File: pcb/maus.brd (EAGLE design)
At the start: 100 x 101 mm, 79 parts, among them IC1 AP1509-50SG-13, J1 SS-52300-001, Q2 BSS123, Q3 BSS123, Q4 BSS123, Q6 PMN30XPEA, Q7 PMN30XPEA, U2 CH340C, U4 LP3965EMP-3.3, U6 LM358DR, U69 ESP32-S2-WROOM

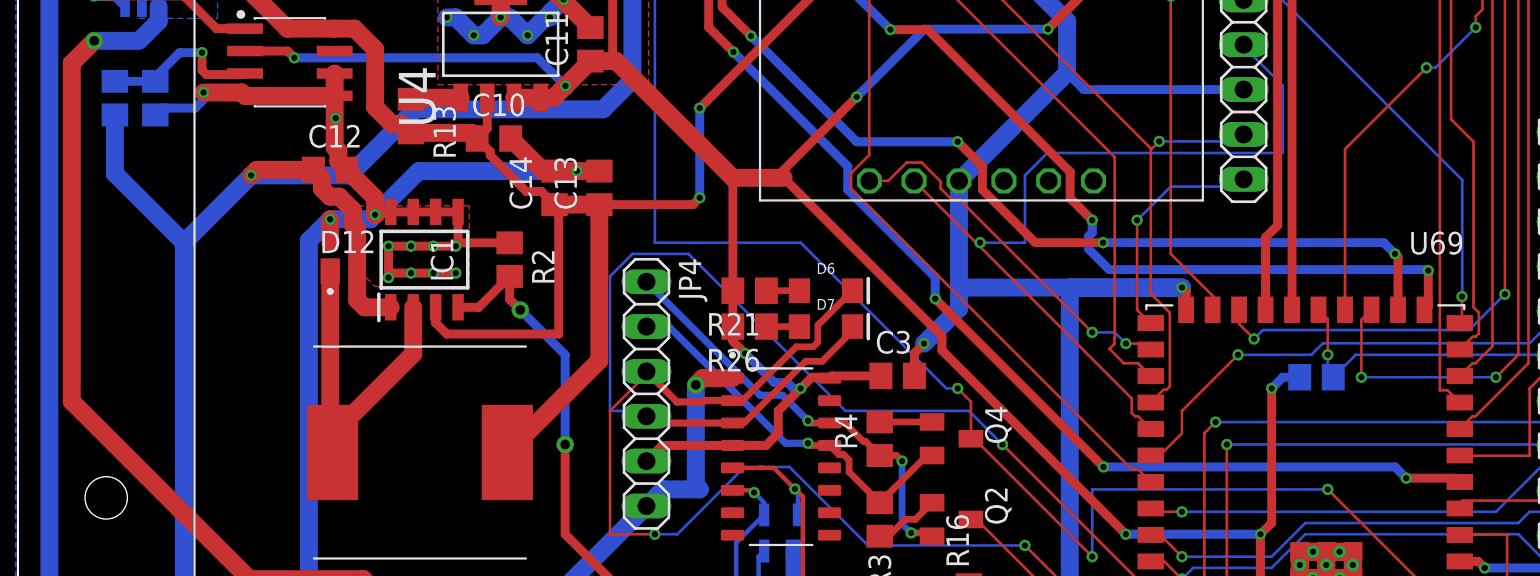
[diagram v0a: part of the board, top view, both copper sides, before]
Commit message: removed wire stubs
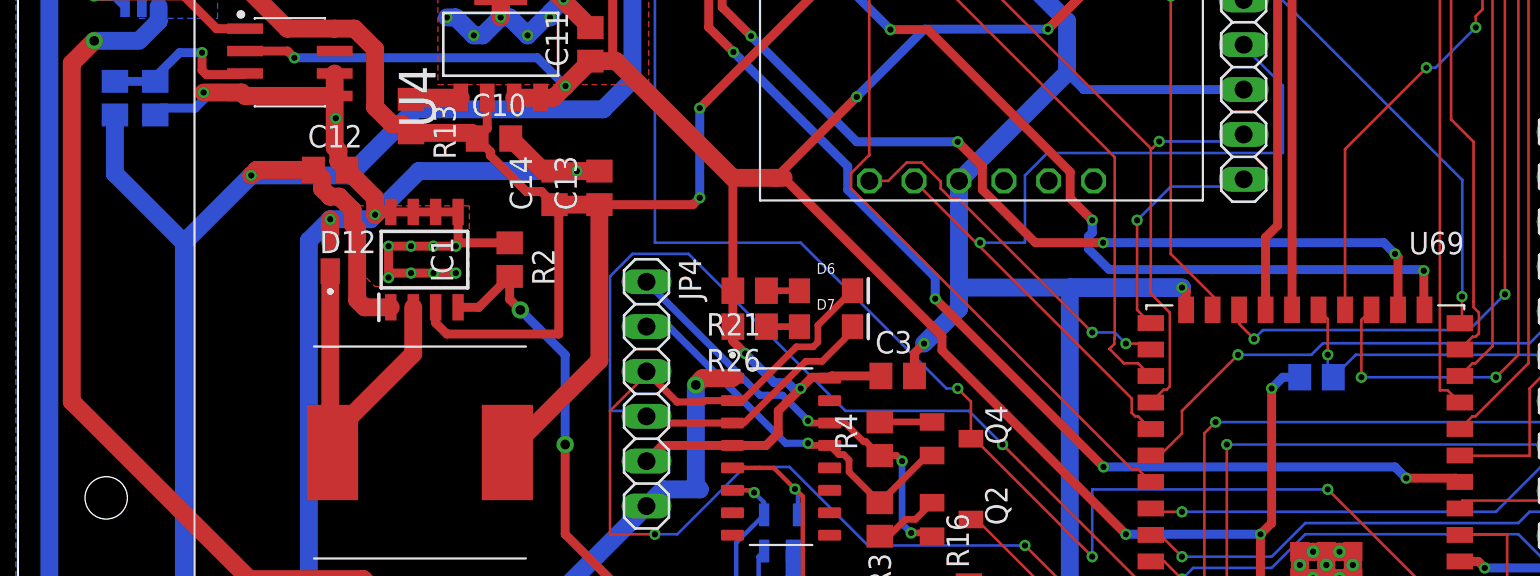
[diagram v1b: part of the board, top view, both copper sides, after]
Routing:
- net ESP32_M2_CH_B: track 51.4 -> 50.7 mm
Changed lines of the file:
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@@
 <wire x1="76.835" y1="45.01204375" x2="76.618" y2="44.79504375" width="0.508" layer="16"/>
 <wire x1="76.618" y1="44.10495625" x2="77.79695625" y2="42.926" width="0.508" layer="16"/>
-<wire x1="95.885" y1="42.8423" x2="95.8648" y2="42.8625" width="0.508" layer="16"/>
-<via x="95.8648" y="42.8625" extent="1-16" drill="0.35"/>
-<wire x1="95.8648" y1="42.8625" x2="95.8648" y2="40.8648" width="0.508" layer="1"/>
-<wire x1="95.8648" y1="40.8648" x2="95.65" y2="40.65" width="0.508" layer="1"/>
-<wire x1="77.79695625" y1="42.926" x2="95.8013" y2="42.926" width="0.508" layer="16"/>
-<wire x1="95.8013" y1="42.926" x2="95.8648" y2="42.8625" width="0.508" layer="16"/>
+<via x="95.6108" y="42.8625" extent="1-16" drill="0.35"/>
+<wire x1="95.65" y1="40.65" x2="95.6108" y2="40.6892" width="0.508" layer="1"/>
+<wire x1="95.6108" y1="42.8625" x2="95.6108" y2="40.6892" width="0.508" layer="1"/>
+<wire x1="77.79695625" y1="42.926" x2="95.5473" y2="42.926" width="0.508" layer="16"/>
+<wire x1="95.5473" y1="42.926" x2="95.6108" y2="42.8625" width="0.508" layer="16"/>
 </signal>
 <signal name="ESP32_M1_2">
@@
 <wire x1="45.085" y1="86.995" x2="71.755" y2="86.995" width="0.15" layer="1"/>
 <wire x1="45.085" y1="86.995" x2="44.85" y2="87.49" width="0.15" layer="1"/>
-<wire x1="85.15" y1="40.2012375" x2="85.15" y2="40.65" width="0.1524" layer="1"/>
 <via x="78.74" y="81.915" extent="1-16" drill="0.35"/>
 <wire x1="85.15" y1="40.65" x2="85.15" y2="39.85" width="0.1524" layer="1"/>
@@
 <wire x1="98.552" y1="57.277" x2="98.552" y2="56.642" width="0.15" layer="1"/>
 <wire x1="95.885" y1="84.455" x2="98.679" y2="84.455" width="0.15" layer="16"/>
-<wire x1="91.44" y1="41.275" x2="91.15" y2="40.65" width="0.15" layer="1"/>
 <wire x1="95.885" y1="84.455" x2="95.5" y2="84.76" width="0.15" layer="16"/>
 <via x="98.679" y="84.455" extent="1-16" drill="0.35"/>
@@
 <contactref element="U2" pad="5"/>
 <wire x1="56.464" y1="31.697" x2="58" y2="31.697" width="0.254" layer="1" grouprefs="USB"/>
-<wire x1="58" y1="31.697" x2="58.198" y2="31.697" width="0.254" layer="1" grouprefs="USB"/>
 <wire x1="60.444" y1="30.086" x2="60.444" y2="22.934" width="0.254" layer="1" grouprefs="USB"/>
 <wire x1="58" y1="31.697" x2="58.803" y2="31.697" width="0.254" layer="1"/>
@@
 <wire x1="29.75" y1="74.93" x2="29.75" y2="68.58" width="0.508" layer="1" grouprefs="MOTOR_LINKS"/>
 <wire x1="87.17" y1="69.19" x2="87.17" y2="75.78" width="0.508" layer="1"/>
-<wire x1="21.494" y1="51.684" x2="21.59" y2="51.588" width="1.016" layer="16"/>
 <wire x1="25.276" y1="19.378" x2="25.4" y2="19.502" width="1.016" layer="16"/>
 <via x="29.21" y="48.26" extent="1-16" drill="0.35"/>

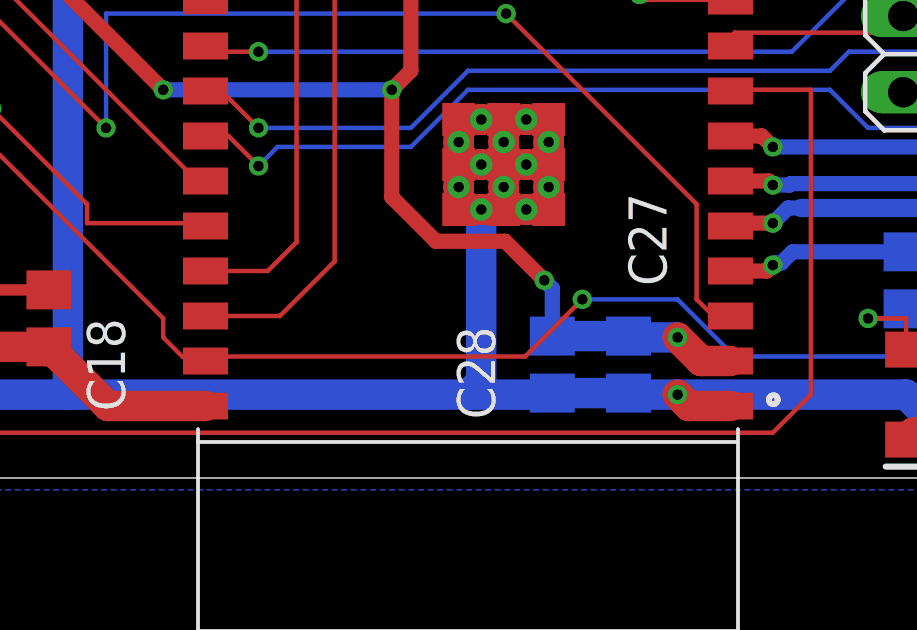
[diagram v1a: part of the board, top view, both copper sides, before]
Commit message: via am C27
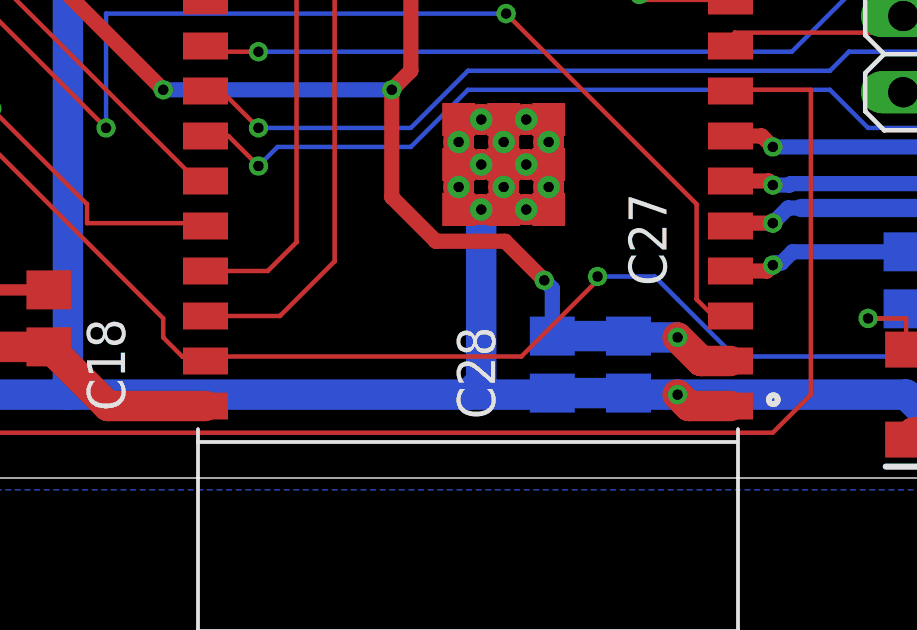
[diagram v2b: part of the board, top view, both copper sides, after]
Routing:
- net ESP32_EN: track 217.9 -> 219.0 mm

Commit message: meeting mit alex
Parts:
- moved YRMOM 14.6 mm to (42.4, 77.0), flipped to the bottom, turned to 90 degrees
- moved D8 13.3 mm to (42.4, 69.2), flipped to the bottom, turned to 90 degrees
- moved SV2 13.2 mm to (42.1, 73.0), turned to 180 degrees
- moved D11 12.3 mm to (47.1, 77.0), flipped to the bottom, turned to 90 degrees
- moved D10 10.8 mm to (47.2, 69.2), flipped to the bottom, turned to 90 degrees
- moved C9 1.92 mm to (55.4, 72.3), flipped to the bottom
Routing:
- net +3V3: track 268.2 -> 227.0 mm
- net M1_M+: track 57.2 -> 20.9 mm, vias 3 -> 0
- net VBAT: track 229.5 -> 195.5 mm, vias 7 -> 8
- net M1_M-: track 54.3 -> 21.0 mm, vias 2 -> 0
- net ESP32_M1_CH_A: track 115.4 -> 88.2 mm
- net GND: track 849.6 -> 826.5 mm, vias 34 -> 32
- net ESP32_M1_CH_B: track 75.8 -> 54.8 mm

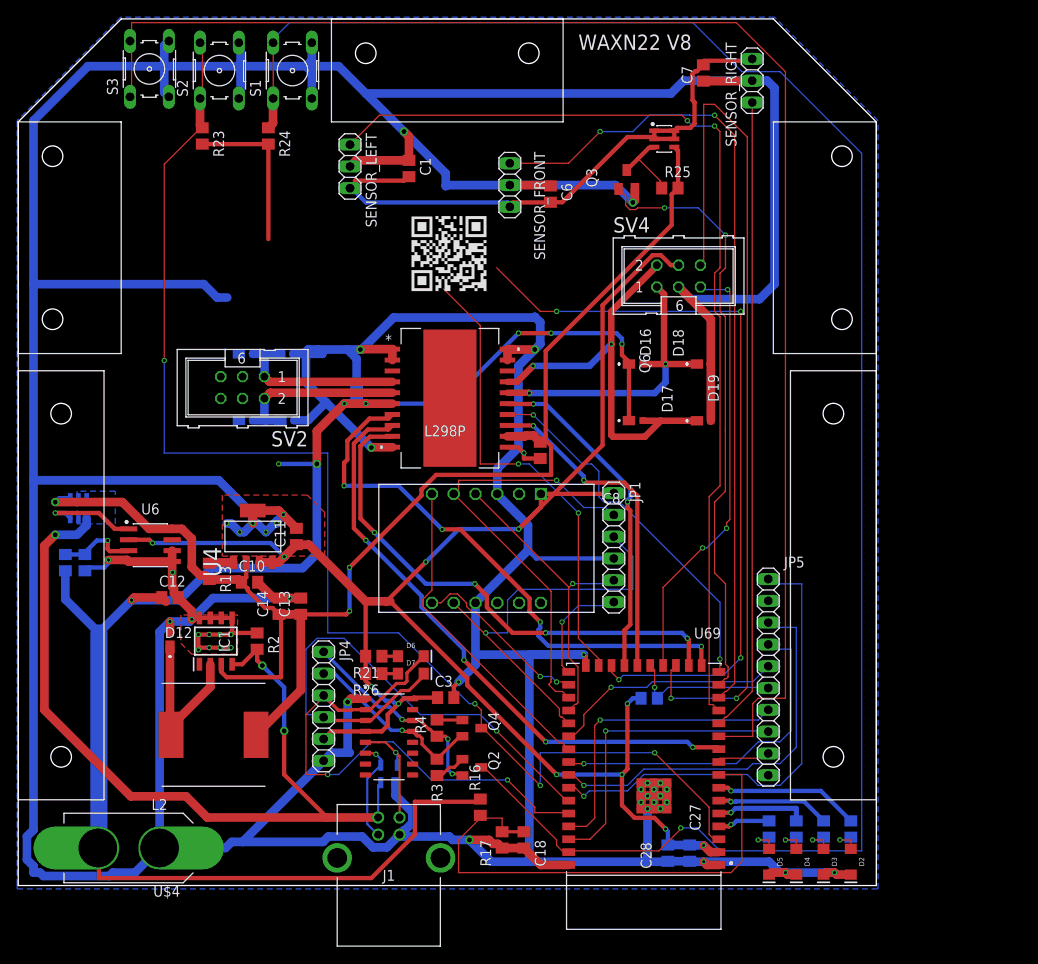
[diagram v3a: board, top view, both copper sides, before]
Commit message: feat: update hbridge, connectors and add motor overlap
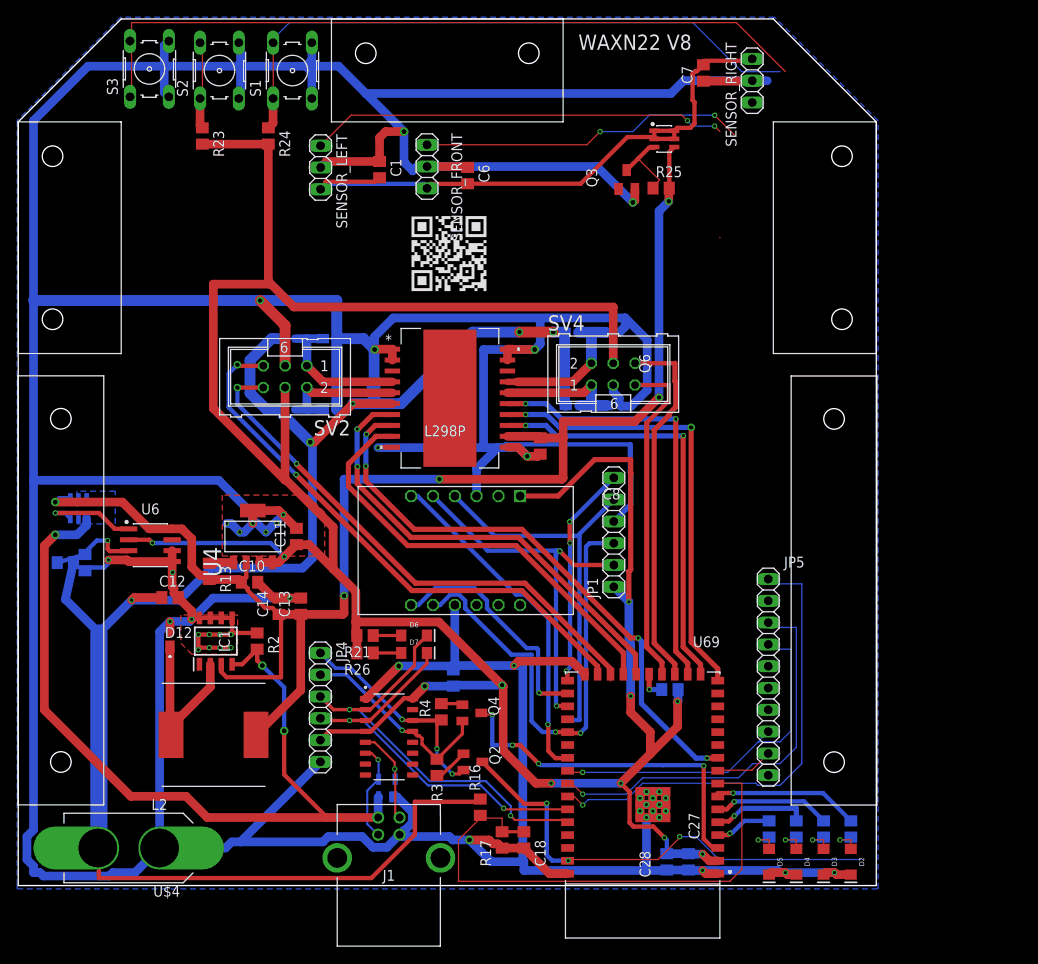
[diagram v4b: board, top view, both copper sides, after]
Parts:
- removed U$5: (no value), shared:MOTOR_HALTERUNG
- added U$3: (no value), maus:MOTOR_HALTERUNG
- moved U$1 50.4 mm to (16.0, 74.4), turned to 270 degrees
- moved D19 14.8 mm to (85.1, 79.5), flipped to the bottom, turned to 90 degrees
- moved SV4 13.7 mm to (85.3, 74.6)
- moved D17 12.7 mm to (80.3, 79.5), flipped to the bottom, turned to 90 degrees
- moved D18 11.6 mm to (85.2, 71.0), flipped to the bottom, turned to 90 degrees
- moved C6 9.89 mm to (68.4, 97.7)
- moved SENSOR_FRONT 9.89 mm to (63.6, 98.8)
- moved D16 8.81 mm to (80.5, 71.0), flipped to the bottom, turned to 90 degrees
- moved D11 5.38 mm to (52.1, 78.7)
- moved YRMOM 5.26 mm to (47.3, 78.7)
- moved SV2 5.11 mm to (47.1, 74.3)
- moved D10 5.11 mm to (52.1, 70.5)
- moved D8 5.11 mm to (47.3, 70.5)
- moved C1 3.43 mm to (58.1, 98.4)
- moved SENSOR_LEFT 3.43 mm to (51.2, 98.7)
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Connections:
- net ESP32_M1_1: now also U69.22; no longer U69.17
- net ESP32_M1_2: now also U69.23; no longer U69.18
- net ESP32_M2_1: now also U69.17; no longer U69.22
- net ESP32_M2_2: now also U69.18; no longer U69.23
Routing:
- net ESP32_IO0: track 154.1 -> 52.2 mm
- net +3V3: track 227.0 -> 322.2 mm
- net ESP32_EN: track 219.0 -> 128.1 mm, vias 1 -> 3
- net N$1: track 172.2 -> 87.5 mm
- net SENSOR_RIGHT: track 74.1 -> 0.00 mm
- net SENSOR_EN: track 70.1 -> 0.00 mm, vias 2 -> 0
- net SENSOR_LEFT: track 114.6 -> 48.8 mm
- net ESP32_M2_CH_A: track 103.2 -> 43.2 mm, vias 2 -> 0
- net SENSOR_FRONT: track 95.9 -> 38.3 mm
- net IO45: track 35.2 -> 0.77 mm, vias 1 -> 0
- net IO46: track 34.8 -> 1.50 mm, vias 1 -> 0
- net M2_M-: track 48.8 -> 17.5 mm, vias 2 -> 0
- net DRDY_M: track 27.4 -> 0.50 mm, vias 1 -> 0
- net ESP32_M1_CH_A: track 88.2 -> 62.7 mm, vias 4 -> 2
- net M2_M+: track 36.7 -> 15.7 mm, vias 2 -> 0
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
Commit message: Connected GPIO and moved around some cablesÇ
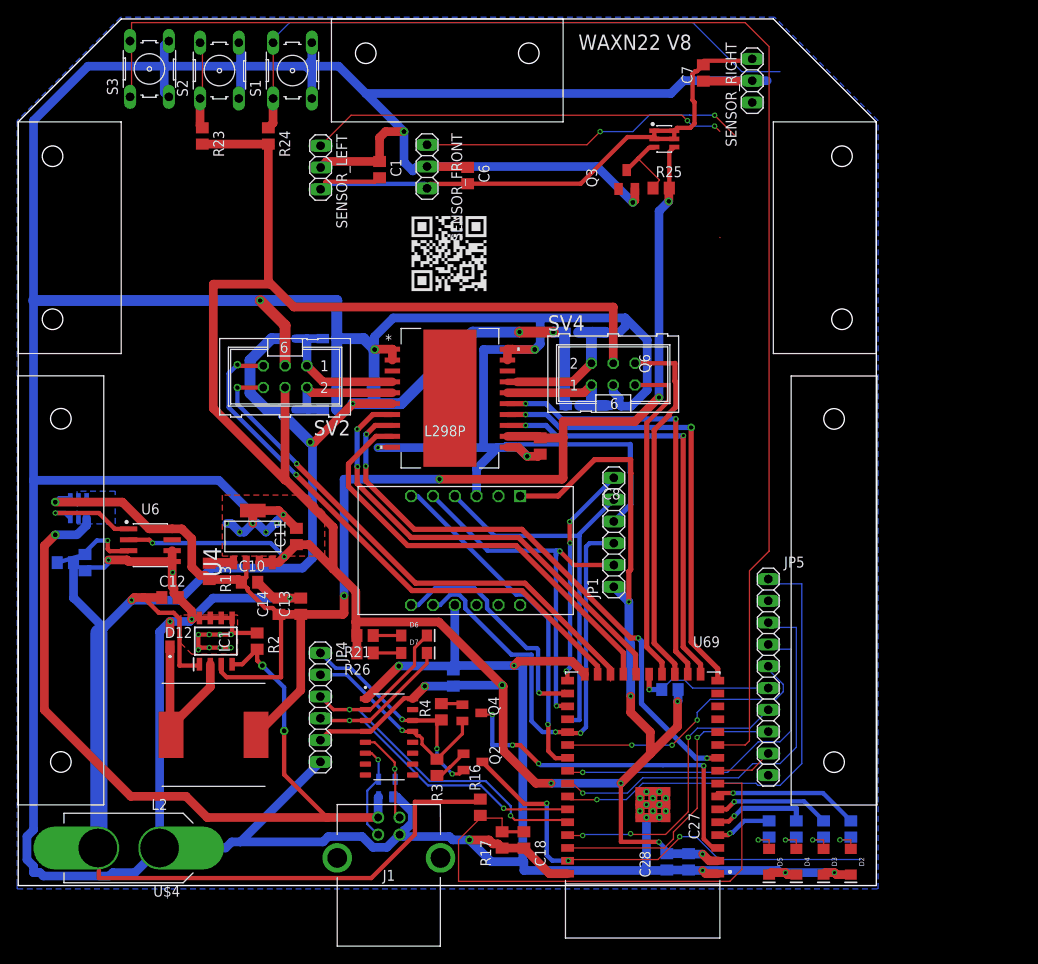
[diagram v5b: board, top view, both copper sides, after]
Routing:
- net N$1: track 87.5 -> 170.1 mm
- net IO45: track 0.77 -> 35.4 mm, vias 0 -> 3
- net IO46: track 1.50 -> 34.3 mm, vias 0 -> 1
- net DRDY_M: track 0.50 -> 32.4 mm, vias 0 -> 3
- net IO18: track 3.26 -> 16.5 mm
- net VBAT: track 201.7 -> 213.9 mm
- net +3V3: track 322.2 -> 323.4 mm
- net DRDY_A/G: track 55.2 -> 54.7 mm

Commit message: Routed more parts. Small problem with left/front/right sensors
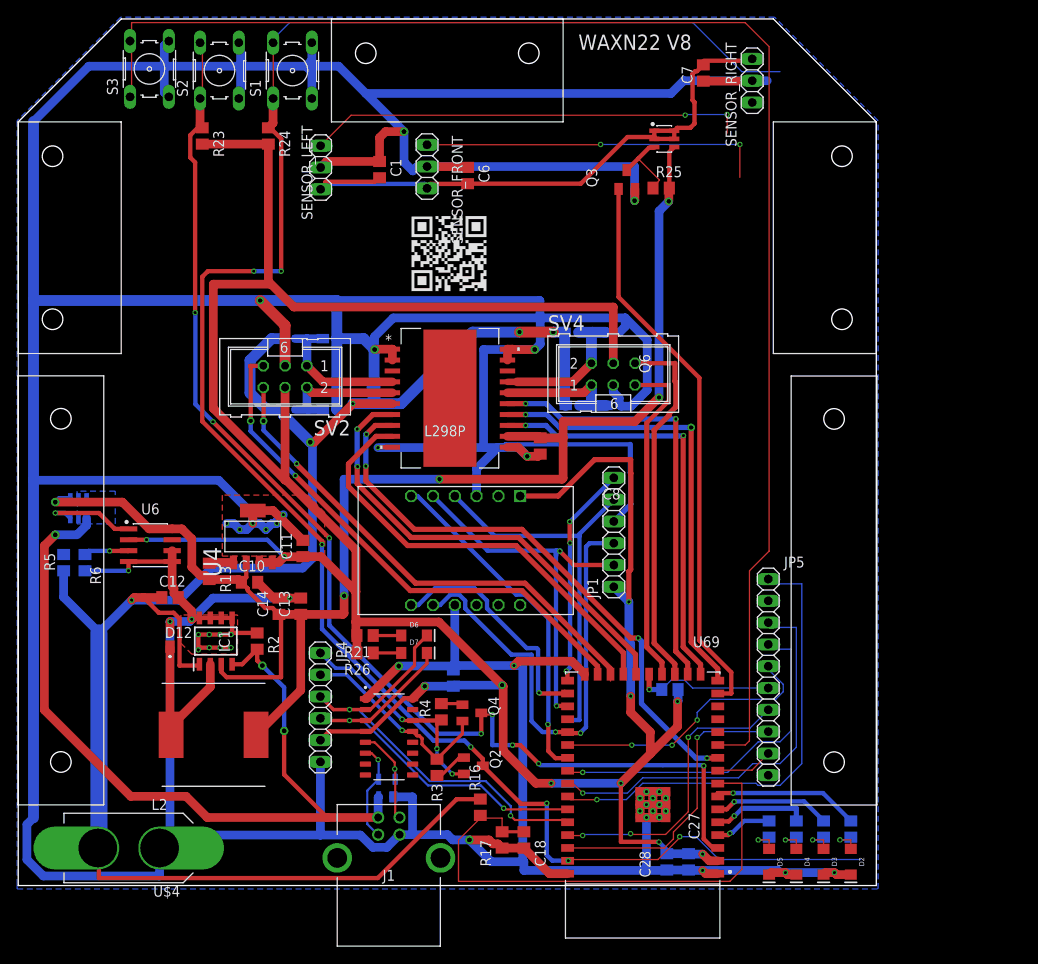
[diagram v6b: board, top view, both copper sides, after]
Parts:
- moved C11 1.59 mm to (49.2, 54.3)
- moved Q2 0.45 mm to (69.0, 29.0)
- moved R5 0.20 mm to (21.3, 52.6), turned to 270 degrees
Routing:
- net ESP32_EN: track 128.1 -> 227.4 mm, vias 3 -> 7
- net ESP32_IO0: track 52.2 -> 143.2 mm, vias 4 -> 8
- net SENSOR_EN: track 0.00 -> 65.8 mm
- net GND: track 821.0 -> 847.8 mm, vias 32 -> 31
- net N$13: track 10.4 -> 5.70 mm
- net ESP32_M1_CH_A: track 62.7 -> 58.5 mm
- net ESP32_M1_CH_B: track 65.2 -> 61.9 mm
- net VBAT: track 213.9 -> 211.5 mm
- net SENSOR_LEFT: track 48.8 -> 51.0 mm
- net SENSOR_FRONT: track 38.3 -> 40.3 mm
- net +3V3: track 323.4 -> 325.2 mm

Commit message: Revert "Routed more parts. Small problem with left/front/right sensors"
This reverts commit 632d98e9f85293ddea98e20d506f01e9db345fa7.
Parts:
- moved C11 1.59 mm to (48.4, 55.7)
- moved Q2 0.45 mm to (69.0, 29.4)
- moved R5 0.20 mm to (21.5, 52.6), turned to 180 degrees
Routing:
- net ESP32_EN: track 227.4 -> 128.1 mm, vias 7 -> 3
- net ESP32_IO0: track 143.2 -> 52.2 mm, vias 8 -> 4
- net SENSOR_EN: track 65.8 -> 0.00 mm
- net GND: track 847.8 -> 821.0 mm, vias 31 -> 32
- net N$13: track 5.70 -> 10.4 mm
- net ESP32_M1_CH_A: track 58.5 -> 62.7 mm
- net ESP32_M1_CH_B: track 61.9 -> 65.2 mm
- net VBAT: track 211.5 -> 213.9 mm
- net SENSOR_LEFT: track 51.0 -> 48.8 mm
- net SENSOR_FRONT: track 40.3 -> 38.3 mm
- net +3V3: track 325.2 -> 323.4 mm
